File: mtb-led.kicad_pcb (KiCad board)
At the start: 2 copper layers, 108 x 51 mm, 57 parts, among them J7 AVR-ISP-6, J9 DEBUG, SW1 SW_Push, U1 ATmega328PB-A, U2 78M05, U3 TLC5940PWP, U4 TLC5940PWP, U5 MAX487E, Y1 14.7456 MHz

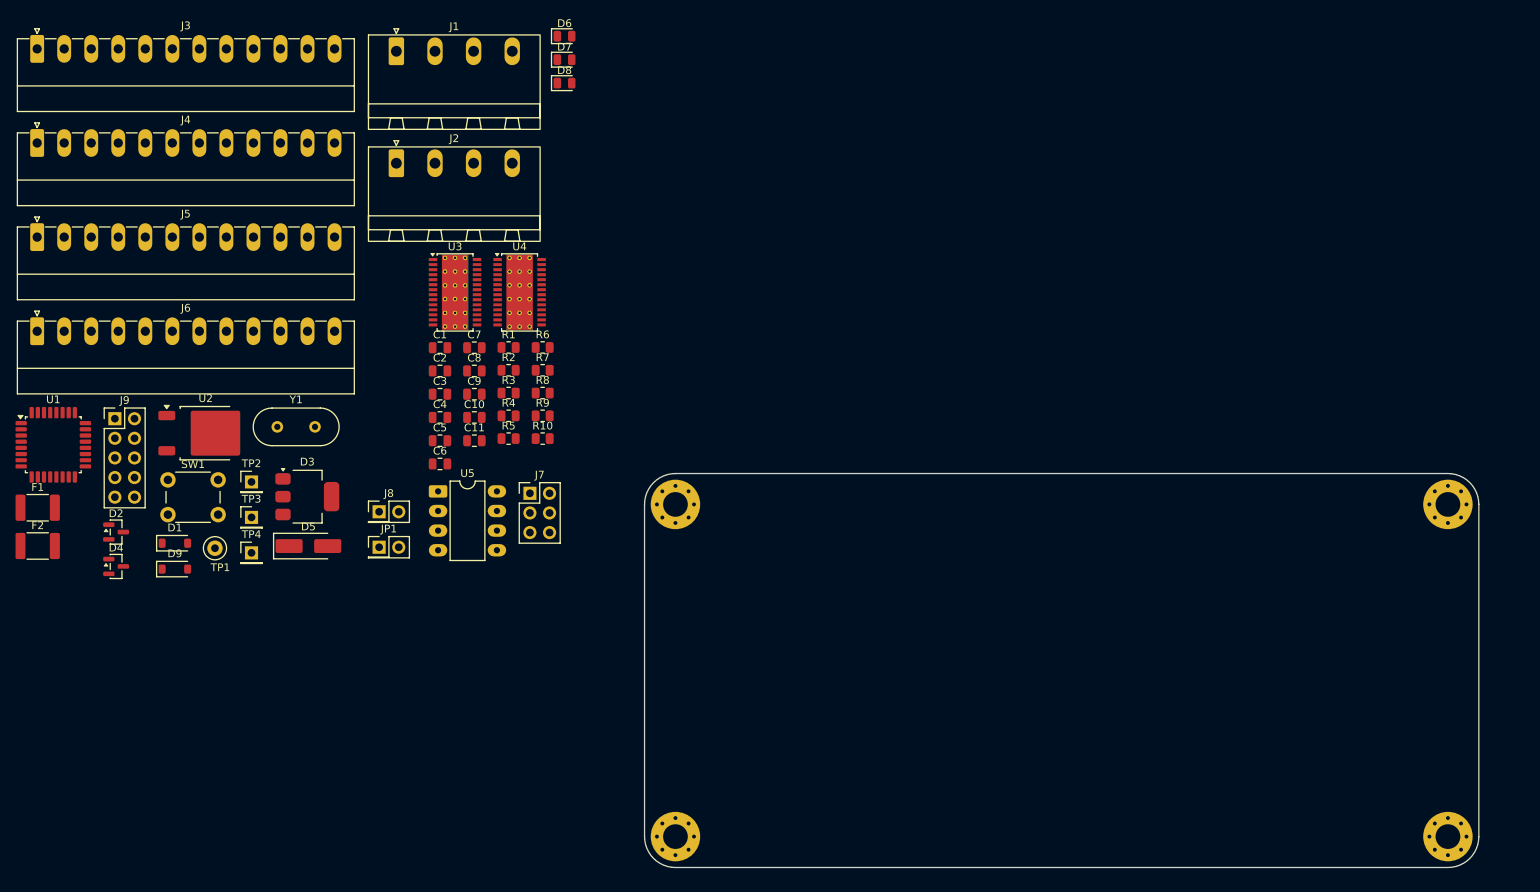
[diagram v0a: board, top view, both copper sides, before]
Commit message: PCB: basic placing of parts.
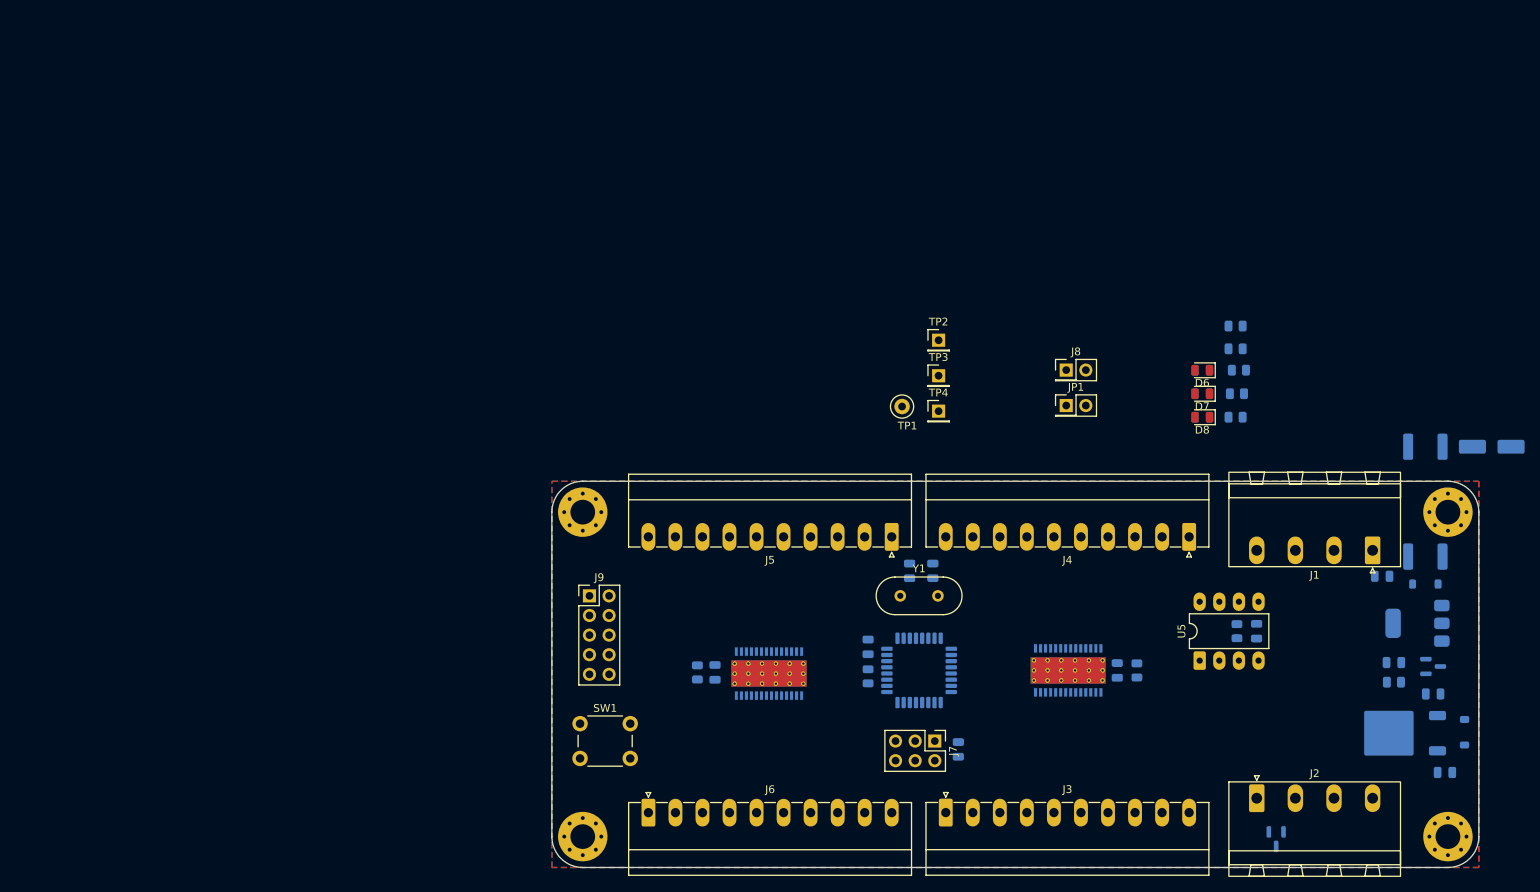
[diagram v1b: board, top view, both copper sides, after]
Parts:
- C1, C10, C11, C2, C3, C4, C5, C6, C7, C8, C9, D1, D2, D3, D4, D5, D9, F1, F2, R1, R10, R2, R3, R4, R5, R6, R7, R8, R9, U1, U2, U3, U4: moved to B.Cu
- J3, J4, J5, J6: footprint Connector_Phoenix_MC:PhoenixContact_MC_1,5_12-G-3.5_1x12_P3.50mm_Horizontal -> Connector_Phoenix_MC:PhoenixContact_MC_1,5_10-G-3.5_1x10_P3.50mm_Horizontal
- moved F2 180.1 mm to (195.1, 65.5)
- moved F1 179.7 mm to (195.1, 79.8), turned to 180 degrees
- moved D2 171.4 mm to (196.1, 94.0)
- moved D9 168.3 mm to (200.2, 102.5), turned to -90 degrees
- moved D1 162.0 mm to (195.1, 83.3), turned to 180 degrees
- moved U2 159.2 mm to (191.6, 102.6), turned to 180 degrees
- moved J4 157.6 mm to (164.5, 77.2), turned to 180 degrees
- moved D4 154.3 mm to (175.8, 116.3), turned to -90 degrees
- moved D5 153.7 mm to (203.7, 65.5), turned to 180 degrees
- moved J3 153.7 mm to (133.0, 112.9)
- moved D3 144.6 mm to (194.1, 88.4), turned to 180 degrees
- moved J1 141.9 mm to (188.2, 78.9), turned to 180 degrees
- moved J2 138.4 mm to (173.2, 111.0)
- moved C4 138.0 mm to (197.6, 107.7)
- moved C3 134.3 mm to (196.1, 97.5), turned to 180 degrees
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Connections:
- J3 pad 2: /OUT0 -> /OUT7
- J3 pad 3: /OUT1 -> /OUT6
- J3 pad 4: /OUT2 -> /OUT5
- J3 pad 5: /OUT3 -> /OUT4
- J3 pad 6: /OUT4 -> /OUT3
- J3 pad 7: /OUT5 -> /OUT2
- J3 pad 8: /OUT6 -> /OUT1
- J3 pad 9: /OUT7 -> /OUT0
- J4 pad 2: /OUT8 -> /OUT15
- J4 pad 3: /OUT9 -> /OUT14
- J4 pad 4: /OUT10 -> /OUT13
- J4 pad 5: /OUT11 -> /OUT12
- J4 pad 6: /OUT12 -> /OUT11
- J4 pad 7: /OUT13 -> /OUT10
- J4 pad 8: /OUT14 -> /OUT9
- J4 pad 9: /OUT15 -> /OUT8
- J5 pad 2: /OUT16 -> /OUT23
- J5 pad 3: /OUT17 -> /OUT22
- J5 pad 4: /OUT18 -> /OUT21
- J5 pad 5: /OUT19 -> /OUT20
- J5 pad 6: /OUT20 -> /OUT19
- J5 pad 7: /OUT21 -> /OUT18
- J5 pad 8: /OUT22 -> /OUT17
- J5 pad 9: /OUT23 -> /OUT16
- J6 pad 2: /OUT24 -> /OUT31
- J6 pad 3: /OUT25 -> /OUT30
- J6 pad 4: /OUT26 -> /OUT29
- J6 pad 5: /OUT27 -> /OUT28
- J6 pad 6: /OUT28 -> /OUT27
- J6 pad 7: /OUT29 -> /OUT26
- J6 pad 8: /OUT30 -> /OUT25
- J6 pad 9: /OUT31 -> /OUT24
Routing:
- added copper zone on B.Cu, net GND
- added copper zone on F.Cu, net GND
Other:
- board size 108 x 51 mm -> 120 x 50 mm

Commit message: PCB: wire, wire, ...
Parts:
- moved SW1 80.0 mm to (165.6, 105.1), turned to 180 degrees
- moved R10 71.5 mm to (117.9, 98.3), turned to -90 degrees
- moved R9 67.0 mm to (117.9, 94.2), turned to -90 degrees
- moved TP1 65.2 mm to (185.7, 89.4)
- moved TP4 59.1 mm to (173.2, 103.4)
- moved TP3 51.0 mm to (165.4, 95.0)
- moved TP2 48.2 mm to (165.4, 86.6)
- moved JP1 44.7 mm to (138.2, 103.6), turned to -90 degrees
- moved J8 42.2 mm to (119.4, 86.1), turned to 90 degrees
- moved R7 41.5 mm to (141.2, 84.6), turned to 90 degrees
- moved R6 39.5 mm to (138.3, 84.6), turned to 90 degrees
- moved D6 38.2 mm to (141.2, 84.6), turned to -90 degrees
- moved R8 37.0 mm to (144.3, 84.6), turned to 90 degrees
- moved D8 36.1 mm to (138.3, 84.6), turned to -90 degrees
- moved D7 33.9 mm to (144.3, 84.6), turned to -90 degrees
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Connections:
- net Net-(U1-PD5) renamed /BTN
- J3 pad 2: /OUT7 -> /OUT15
- J3 pad 3: /OUT6 -> /OUT14
- J3 pad 4: /OUT5 -> /OUT13
- J3 pad 5: /OUT4 -> /OUT12
- J3 pad 6: /OUT3 -> /OUT11
- J3 pad 7: /OUT2 -> /OUT10
- J3 pad 8: /OUT1 -> /OUT9
- J3 pad 9: /OUT0 -> /OUT8
- J4 pad 2: /OUT15 -> /OUT7
- J4 pad 3: /OUT14 -> /OUT6
- J4 pad 4: /OUT13 -> /OUT5
- J4 pad 5: /OUT12 -> /OUT4
- J4 pad 6: /OUT11 -> /OUT3
- J4 pad 7: /OUT10 -> /OUT2
- J4 pad 8: /OUT9 -> /OUT1
- J4 pad 9: /OUT8 -> /OUT0
- J5 pad 2: /OUT23 -> /OUT31
- J5 pad 3: /OUT22 -> /OUT30
- J5 pad 4: /OUT21 -> /OUT29
- J5 pad 5: /OUT20 -> /OUT28
- J5 pad 6: /OUT19 -> /OUT27
- J5 pad 7: /OUT18 -> /OUT26
- J5 pad 8: /OUT17 -> /OUT25
- J5 pad 9: /OUT16 -> /OUT24
- J6 pad 2: /OUT31 -> /OUT23
- J6 pad 3: /OUT30 -> /OUT22
- J6 pad 4: /OUT29 -> /OUT21
- J6 pad 5: /OUT28 -> /OUT20
- J6 pad 6: /OUT27 -> /OUT19
- J6 pad 7: /OUT26 -> /OUT18
- J6 pad 8: /OUT25 -> /OUT17
- J6 pad 9: /OUT24 -> /OUT16
- J9 pad 1: /VPRG -> /DCPRG
- J9 pad 2: /XLAT -> /GSCLK
- J9 pad 3: /DCPRG -> /XLAT
- J9 pad 5: /GSCLK -> /VPRG
- J9 pad 7: /BLANK -> /MOSI
- J9 pad 8: /MOSI -> /BLANK
- U1 pad 11: unconnected-(U1-PD7-Pad11) -> /LED_RED
- U1 pad 23: /LED_RED -> unconnected-(U1-PC0-Pad23)
- U1 pad 26: /BLANK -> /XLAT
- U1 pad 27: /XLAT -> /BLANK
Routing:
- net +12V: track 0.00 -> 233.1 mm
- net +5V: track 0.00 -> 200.2 mm, vias 0 -> 8
- net /MOSI: track 0.00 -> 69.1 mm, vias 0 -> 2
- net /VPRG: track 0.00 -> 67.5 mm, vias 0 -> 3
- net /MTB-DE: track 0.00 -> 67.3 mm, vias 0 -> 2
- net /SCK: track 0.00 -> 66.2 mm, vias 0 -> 4
- net /MTB-TX: track 0.00 -> 63.2 mm, vias 0 -> 2
- net /XLAT: track 0.00 -> 62.3 mm, vias 0 -> 3
- net /BLANK: track 0.00 -> 60.9 mm, vias 0 -> 3
- net /XERR: track 0.00 -> 60.9 mm, vias 0 -> 4
- net /DCPRG: track 0.00 -> 60.2 mm, vias 0 -> 4
- net /GSCLK: track 0.00 -> 58.0 mm, vias 0 -> 4
- net /MTB-RX: track 0.00 -> 54.8 mm, vias 0 -> 2
- net /+12V-IN: track 0.00 -> 54.4 mm
- net /BUS-: track 0.00 -> 52.2 mm, vias 0 -> 1
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
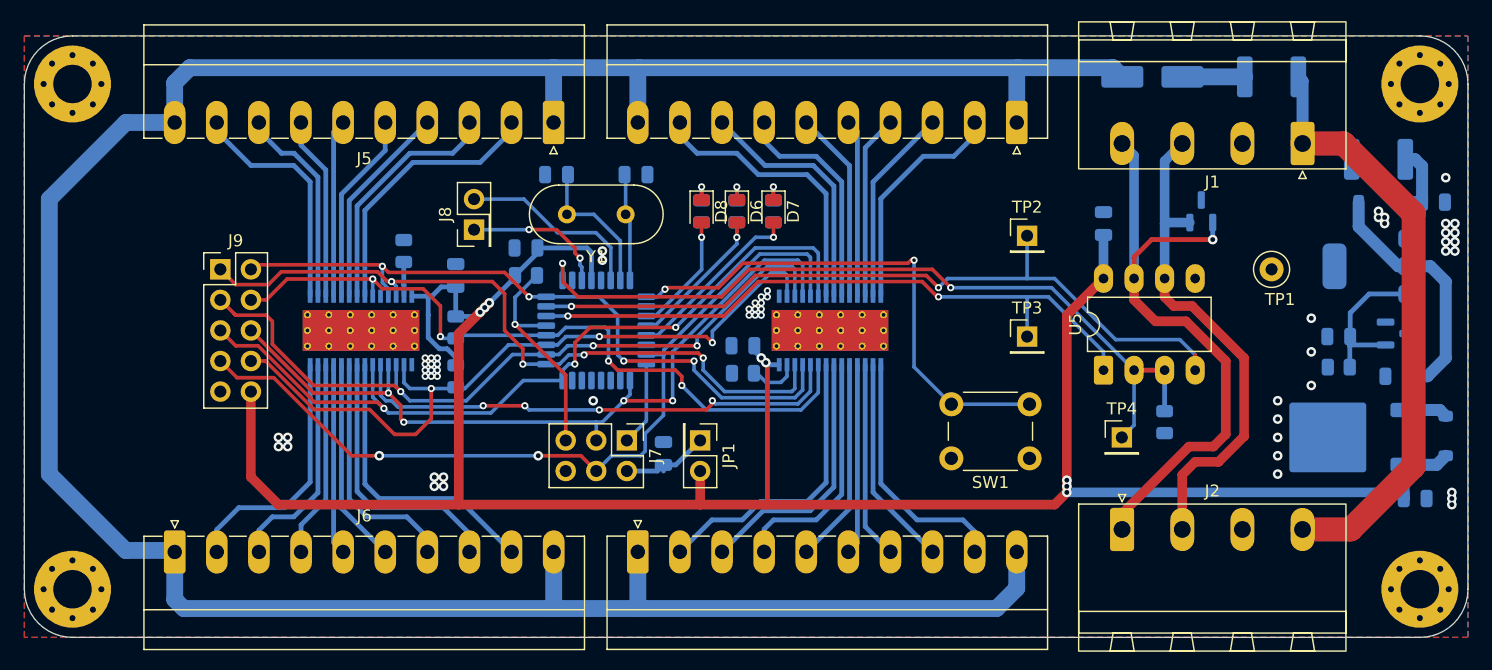
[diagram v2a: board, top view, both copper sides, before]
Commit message: Tweak silkscreen.
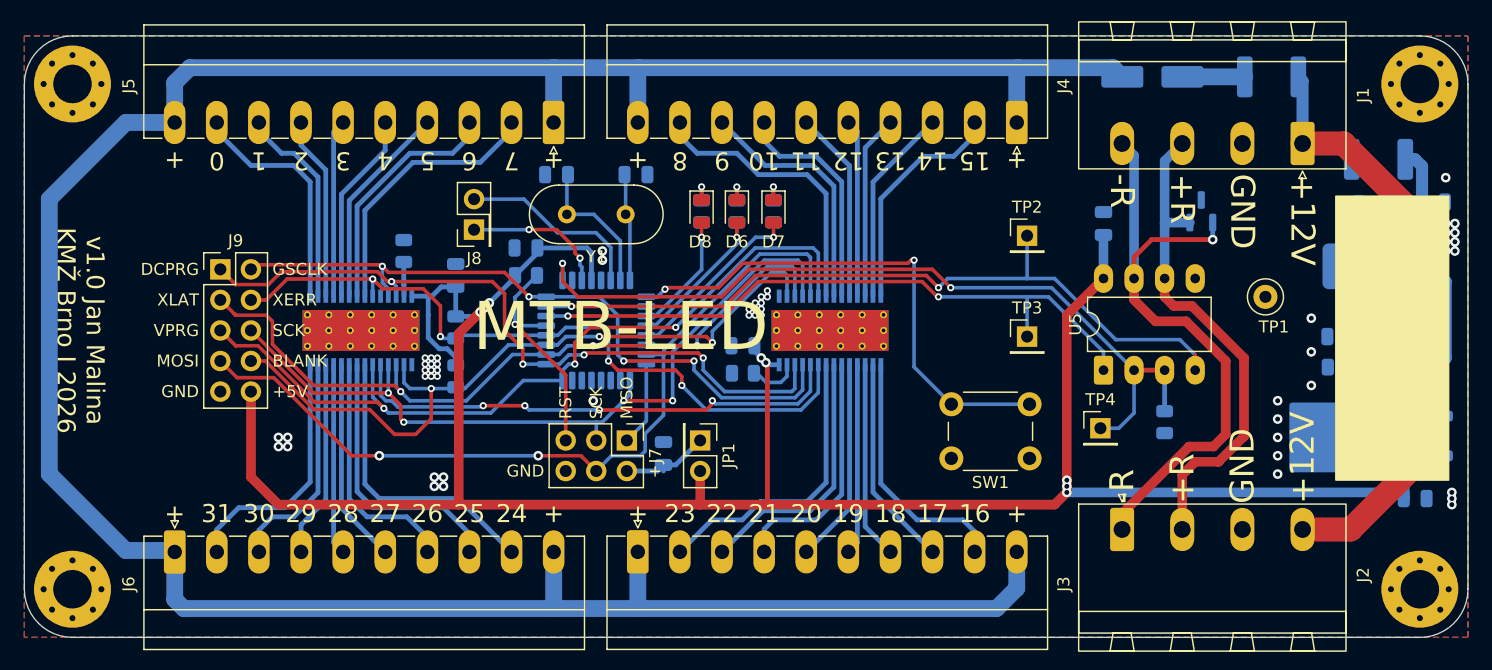
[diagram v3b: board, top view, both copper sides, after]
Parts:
- moved TP1 2.34 mm to (185.2, 91.7)
- moved TP4 1.93 mm to (171.4, 102.6)
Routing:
- net /MTB-DE: track 67.3 -> 68.2 mm
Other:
- board text added: "+"
- board text added: "+12V"
- board text added: "+5V"
- board text added: "+R"
- board text added: "-R"
- board text added: "0"
- board text added: "1"
- board text added: "10"
- board text added: "11"
- board text added: "12"
- board text added: "13"
- board text added: "14"
- board text added: "15"
- board text added: "16"
- board text added: "17"
- board text added: "18"
- board text added: "19"
- board text added: "2"
- board text added: "20"
- board text added: "21"
- board text added: "22"
- board text added: "23"
- board text added: "24"
- board text added: "25"
- board text added: "26"
- board text added: "27"
- board text added: "28"
- board text added: "29"
- board text added: "3"
- board text added: "30"
- board text added: "31"
- board text added: "4"
- board text added: "5"
- board text added: "6"
- board text added: "7"
- board text added: "8"
- board text added: "9"
- board text added: "BLANK"
- board text added: "DCPRG"
- board text added: "GND"
- board text added: "GSCLK"
- board text added: "MISO"
- board text added: "MOSI"
- board text added: "MTB-LED"
- board text added: "RST"
- board text added: "SCK"
- board text added: "VPRG"
- board text added: "XERR"
- board text added: "XLAT"
- board text added: "v1.0 Jan Malina KMŽ Brno I 2026"

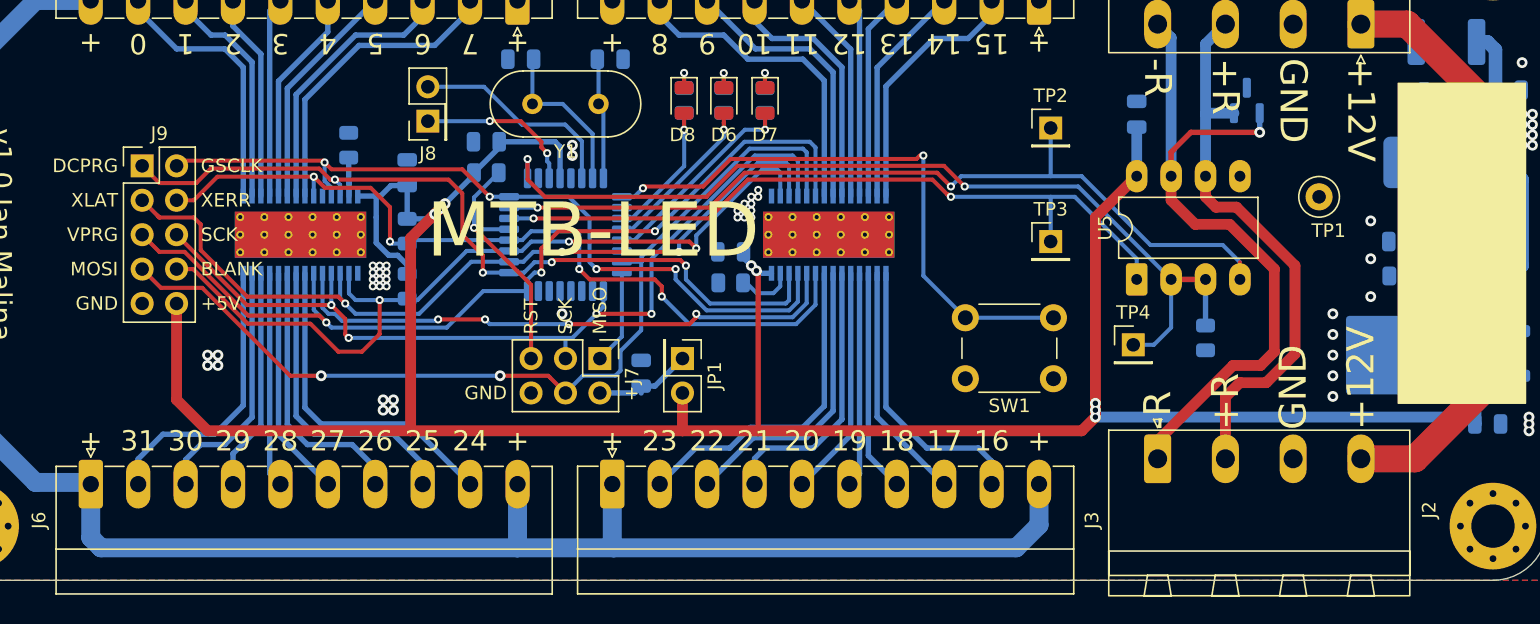
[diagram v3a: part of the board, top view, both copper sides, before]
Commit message: PCB: add GND vias.
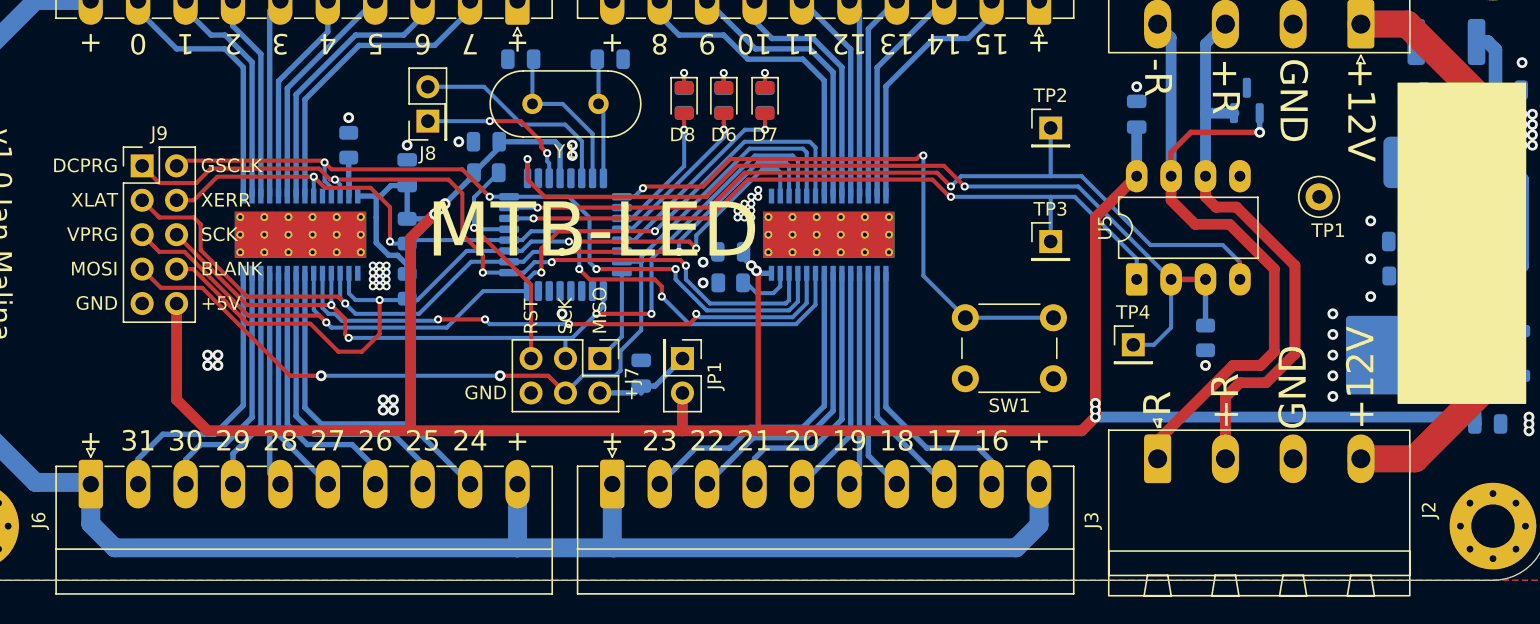
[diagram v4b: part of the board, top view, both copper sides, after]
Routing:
- net +12V: track 233.1 -> 232.5 mm
- net GND: vias 58 -> 67
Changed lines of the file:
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@@
+	)
+	(via
+		(at 121.666 87.63)
+		(size 0.8)
+		(drill 0.4)
+		(layers "F.Cu" "B.Cu")
+		(free yes)
+		(net 2)
 	)
 	(via
@@
 	)
 	(via
+		(at 139.7 98.044)
+		(size 0.8)
+		(drill 0.4)
+		(layers "F.Cu" "B.Cu")
+		(free yes)
+		(net 2)
+	)
+	(via
 		(at 200.66 108.966)
 		(size 0.8)
@@
 	)
 	(via
+		(at 195.072 86.106)
+		(size 0.8)
+		(drill 0.4)
+		(layers "F.Cu" "B.Cu")
+		(free yes)
+		(net 2)
+	)
+	(via
 		(at 116.332 96.774)
 		(size 0.6)
@@
 	)
 	(via
+		(at 193.802 98.298)
+		(size 0.8)
+		(drill 0.4)
+		(layers "F.Cu" "B.Cu")
+		(free yes)
+		(net 2)
+	)
+	(via
 		(at 200.152 85.598)
 		(size 0.8)
@@
 	)
 	(via
+		(at 139.7 96.52)
+		(size 0.8)
+		(drill 0.4)
+		(layers "F.Cu" "B.Cu")
+		(free yes)
+		(net 2)
+	)
+	(via
 		(at 115.824 98.298)
 		(size 0.6)
@@
 	)
 	(via
+		(at 113.538 85.852)
+		(size 0.8)
+		(drill 0.4)
+		(layers "F.Cu" "B.Cu")
+		(free yes)
+		(net 2)
+	)
+	(via
 		(at 115.316 96.774)
 		(size 0.6)
@@
 	)
 	(via
+		(at 176.784 104.14)
+		(size 0.8)
+		(drill 0.4)
+		(layers "F.Cu" "B.Cu")
+		(free yes)
+		(net 2)
+	)
+	(via
 		(at 116.078 106.68)
 		(size 0.8)
@@
 	)
 	(via
+		(at 171.704 83.566)
+		(size 0.8)
+		(drill 0.4)
+		(layers "F.Cu" "B.Cu")
+		(free yes)
+		(net 2)
+	)
+	(via
 		(at 142.748 92.71)
 		(size 0.6)
@@
 	(via
 		(at 200.914 86.36)
+		(size 0.8)
+		(drill 0.4)
+		(layers "F.Cu" "B.Cu")
+		(free yes)
+		(net 2)
+	)
+	(via
+		(at 117.856 87.884)
 		(size 0.8)
 		(drill 0.4)
@@
 	)
 	(segment
-		(start 94.5 116.852)
-		(end 95.25 117.602)
+		(start 94.5 115.836)
+		(end 96.266 117.602)
 		(width 1.4)
 		(layer "B.Cu")
@@
 	)
 	(segment
+		(start 94.5 112.9)
+		(end 94.5 115.836)
+		(width 1.4)
+		(layer "B.Cu")
+		(net 12)
+	)
+	(segment
 		(start 133.096 72.644)
 		(end 125.984 72.644)
@@
 	)
 	(segment
-		(start 95.25 117.602)
-		(end 125.984 117.602)
-		(width 1.4)
-		(layer "B.Cu")
-		(net 12)
-	)
-	(segment
 		(start 164.592 72.644)
 		(end 133.096 72.644)
@@
 	)
 	(segment
+		(start 96.266 117.602)
+		(end 125.984 117.602)
+		(width 1.4)
+		(layer "B.Cu")
+		(net 12)
+	)
+	(segment
 		(start 125.984 117.602)
 		(end 133.096 117.602)
@@
 		(width 1.4)
 		(layer "B.Cu")
-		(net 12)
-	)
-	(segment
-		(start 94.5 112.9)
-		(end 94.5 116.852)
-		(width 1.4)
-		(layer "B.Cu")
